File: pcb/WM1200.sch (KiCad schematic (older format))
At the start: 0 parts

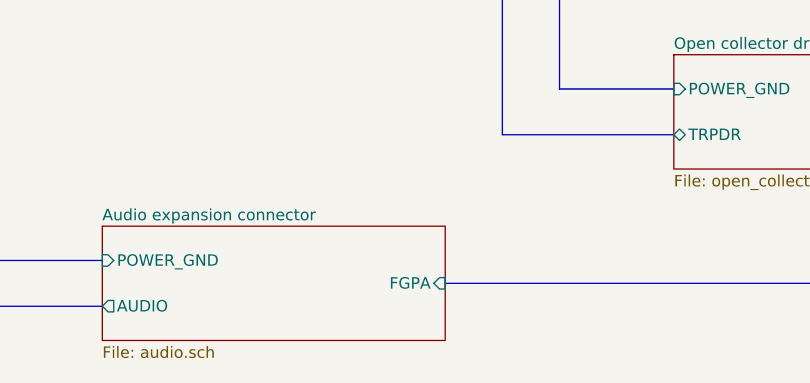
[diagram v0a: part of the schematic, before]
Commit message: bus name typo fixed on audio sheet
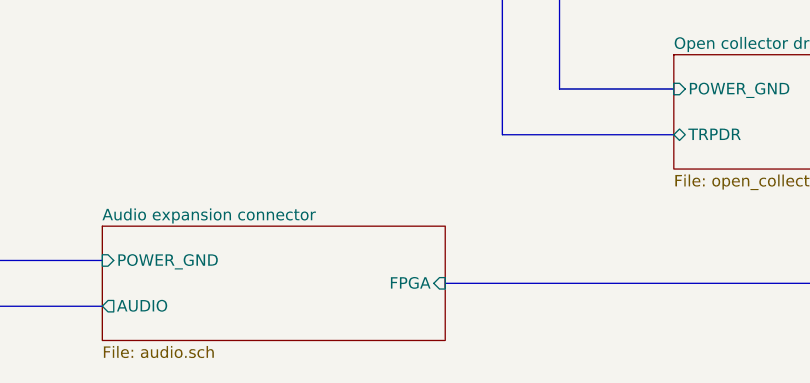
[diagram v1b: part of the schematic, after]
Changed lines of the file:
@@
 	5500 1150 5500 1650
-$Sheet
-S 3500 5250 1500 500
-U 5E5BC361
-F0 "Audio expansion connector" 50
-F1 "audio.sch" 50
-F2 "AUDIO" O L 3500 5600 50
-F3 "FGPA" I R 5000 5500 50
-F4 "POWER_GND" I L 3500 5400 50
-$EndSheet
 $Sheet
 S 6000 1500 1450 500
@@
 	3000 5400 3500 5400
 Connection ~ 3000 3750
+$Sheet
+S 3500 5250 1500 500
+U 5E5BC361
+F0 "Audio expansion connector" 50
+F1 "audio.sch" 50
+F2 "AUDIO" O L 3500 5600 50
+F3 "POWER_GND" I L 3500 5400 50
+F4 "FPGA" I R 5000 5500 50
+$EndSheet
 $EndSCHEMATC

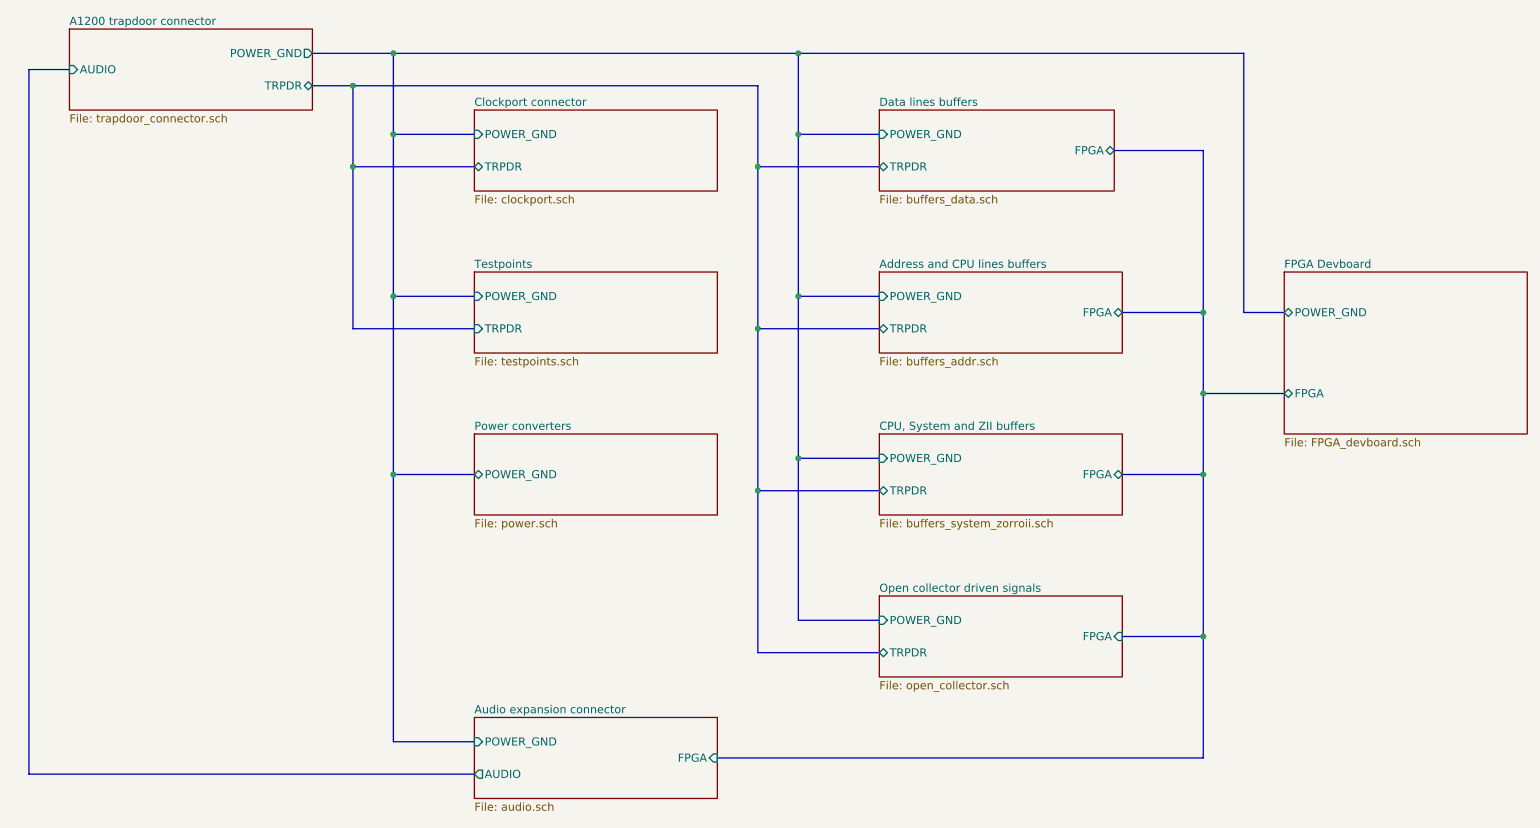
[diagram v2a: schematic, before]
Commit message: The scheme needs it's buses to be remade because of the way KiCad works, ok
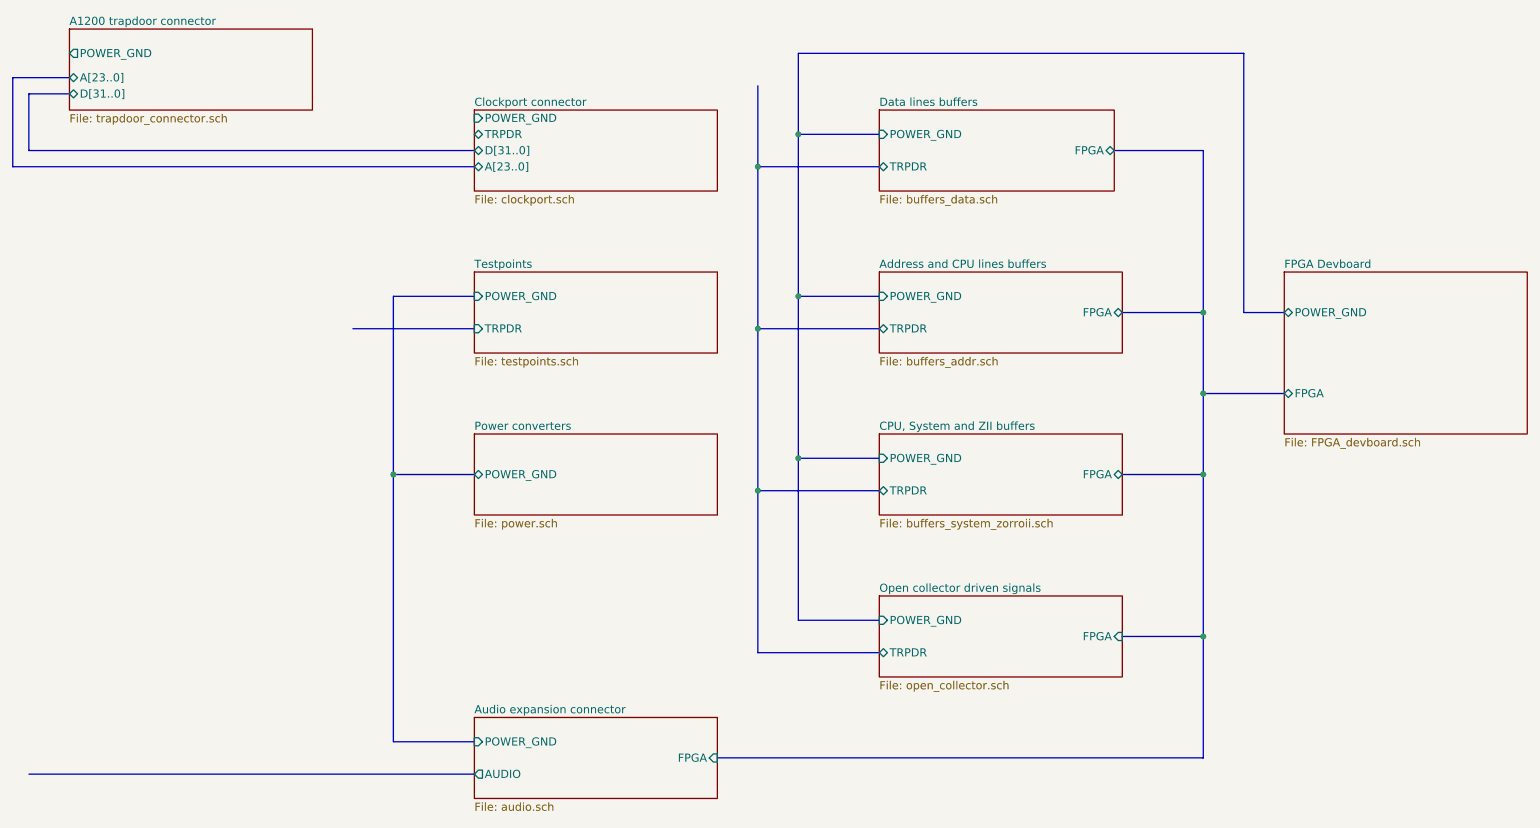
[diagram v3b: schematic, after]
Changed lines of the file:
@@
 F0 "A1200 trapdoor connector" 50
 F1 "trapdoor_connector.sch" 50
-F2 "AUDIO" I L 1000 1250 50
-F3 "POWER_GND" O R 2500 1150 50
-F4 "TRPDR" B R 2500 1350 50
-$EndSheet
-$Sheet
-S 3500 1500 1500 500
-U 5E55E8C3
-F0 "Clockport connector" 50
-F1 "clockport.sch" 50
-F2 "POWER_GND" I L 3500 1650 50
-F3 "TRPDR" B L 3500 1850 50
+F2 "POWER_GND" O L 1000 1150 50
+F3 "A[23..0]" B L 1000 1300 50
+F4 "D[31..0]" B L 1000 1400 50
 $EndSheet
 $Sheet
@@
 F3 "TRPDR" I L 3500 2850 50
 $EndSheet
-Wire Bus Line
-	3000 1650 3500 1650
 $Sheet
 S 6000 4500 1500 500
@@
 F4 "POWER_GND" I L 6000 3650 50
 $EndSheet
-Wire Bus Line
-	1000 1250 750  1250
-Wire Bus Line
-	750  1250 750  5600
 Wire Bus Line
 	750  5600 3500 5600
@@
 	8000 3250 8000 3750
 Wire Bus Line
-	3000 1650 3000 2650
-Wire Bus Line
 	5500 4650 6000 4650
 Wire Bus Line
@@
 	3500 2650 3000 2650
 Wire Bus Line
-	2500 1150 3000 1150
-Wire Bus Line
 	5500 1150 8250 1150
 Wire Bus Line
 	8250 1150 8250 2750
-Connection ~ 5500 1150
-Wire Bus Line
-	2750 1350 5250 1350
-Wire Bus Line
-	3000 1650 3000 1150
-Connection ~ 3000 1650
-Connection ~ 3000 1150
-Wire Bus Line
-	3000 1150 5500 1150
 Wire Bus Line
 	3000 2650 3000 3750
 Wire Bus Line
 	3000 3750 3500 3750
-Connection ~ 3000 2650
 Wire Bus Line
 	3000 3750 3000 5400
@@
 F4 "FPGA" I R 5000 5500 50
 $EndSheet
+$Sheet
+S 3500 1500 1500 500
+U 5E55E8C3
+F0 "Clockport connector" 50
+F1 "clockport.sch" 50
+F2 "POWER_GND" I L 3500 1550 50
+F3 "TRPDR" B L 3500 1650 50
+F4 "D[31..0]" B L 3500 1750 50
+F5 "A[23..0]" B L 3500 1850 50
+$EndSheet
 Wire Bus Line
-	2750 1850 3500 1850
+	1000 1300 650  1300
 Wire Bus Line
-	2750 1850 2750 2850
-Connection ~ 2750 1850
+	650  1300 650  1850
 Wire Bus Line
-	2750 1850 2750 1350
-Connection ~ 2750 1350
+	650  1850 3500 1850
 Wire Bus Line
-	2500 1350 2750 1350
+	1000 1400 750  1400
+Wire Bus Line
+	750  1400 750  1750
+Wire Bus Line
+	750  1750 3500 1750
 $EndSCHEMATC

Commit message: wip commit (sync work between pc's)
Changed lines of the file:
@@
 $EndDescr
-$Sheet
-S 1000 1000 1500 500
-U 5E6286C8
-F0 "A1200 trapdoor connector" 50
-F1 "trapdoor_connector.sch" 50
-F2 "POWER_GND" O L 1000 1150 50
-F3 "A[23..0]" B L 1000 1300 50
-F4 "D[31..0]" B L 1000 1400 50
-$EndSheet
 $Sheet
 S 3500 2500 1500 500
@@
 F5 "A[23..0]" B L 3500 1850 50
 $EndSheet
-Wire Bus Line
-	1000 1300 650  1300
-Wire Bus Line
-	650  1300 650  1850
-Wire Bus Line
-	650  1850 3500 1850
-Wire Bus Line
-	1000 1400 750  1400
-Wire Bus Line
-	750  1400 750  1750
-Wire Bus Line
-	750  1750 3500 1750
+$Sheet
+S 1000 1000 1500 2500
+U 5E6286C8
+F0 "A1200 trapdoor connector" 50
+F1 "trapdoor_connector.sch" 50
+F2 "A[23..0]" B R 2500 1100 50
+F3 "D[31..0]" B R 2500 1200 50
+F4 "_IPL[2..0]" B R 2500 1400 50
+F5 "SIZE[1..0]" B R 2500 1500 50
+F6 "_DSACK[1..0]" B R 2500 1600 50
+F7 "FC[2..0]" B R 2500 1700 50
+F8 "_RST" B R 2500 1800 50
+F9 "_HLT" B R 2500 1900 50
+F10 "_AS" B R 2500 2000 50
+F11 "_DS" B R 2500 2100 50
+F12 "R_W" B R 2500 2200 50
+F13 "_BERR" B R 2500 2300 50
+F14 "CPUCLK_A" B R 2500 2400 50
+F15 "E_CLOCK" B R 2500 2500 50
+F16 "_BR" B R 2500 2600 50
+F17 "_BOSS" B R 2500 2700 50
+F18 "CCKA" B R 2500 2800 50
+F19 "_RESET" B R 2500 2900 50
+F20 "_SPARECS" B R 2500 3000 50
+F21 "_RTCCS" B R 2500 3100 50
+F22 "_KBRESET" B R 2500 3200 50
+F23 "_IORD" B R 2500 3300 50
+F24 "AUDIO_RIGHT" B R 2500 3400 50
+F25 "AUDIO_LEFT" B L 1000 3200 50
+F26 "AUDIO_GND" B L 1000 3100 50
+F27 "_INT6" B L 1000 3000 50
+F28 "_INT2" B L 1000 2900 50
+F29 "_OVR" B L 1000 2800 50
+F30 "_IOWR" B L 1000 2700 50
+$EndSheet
 $EndSCHEMATC

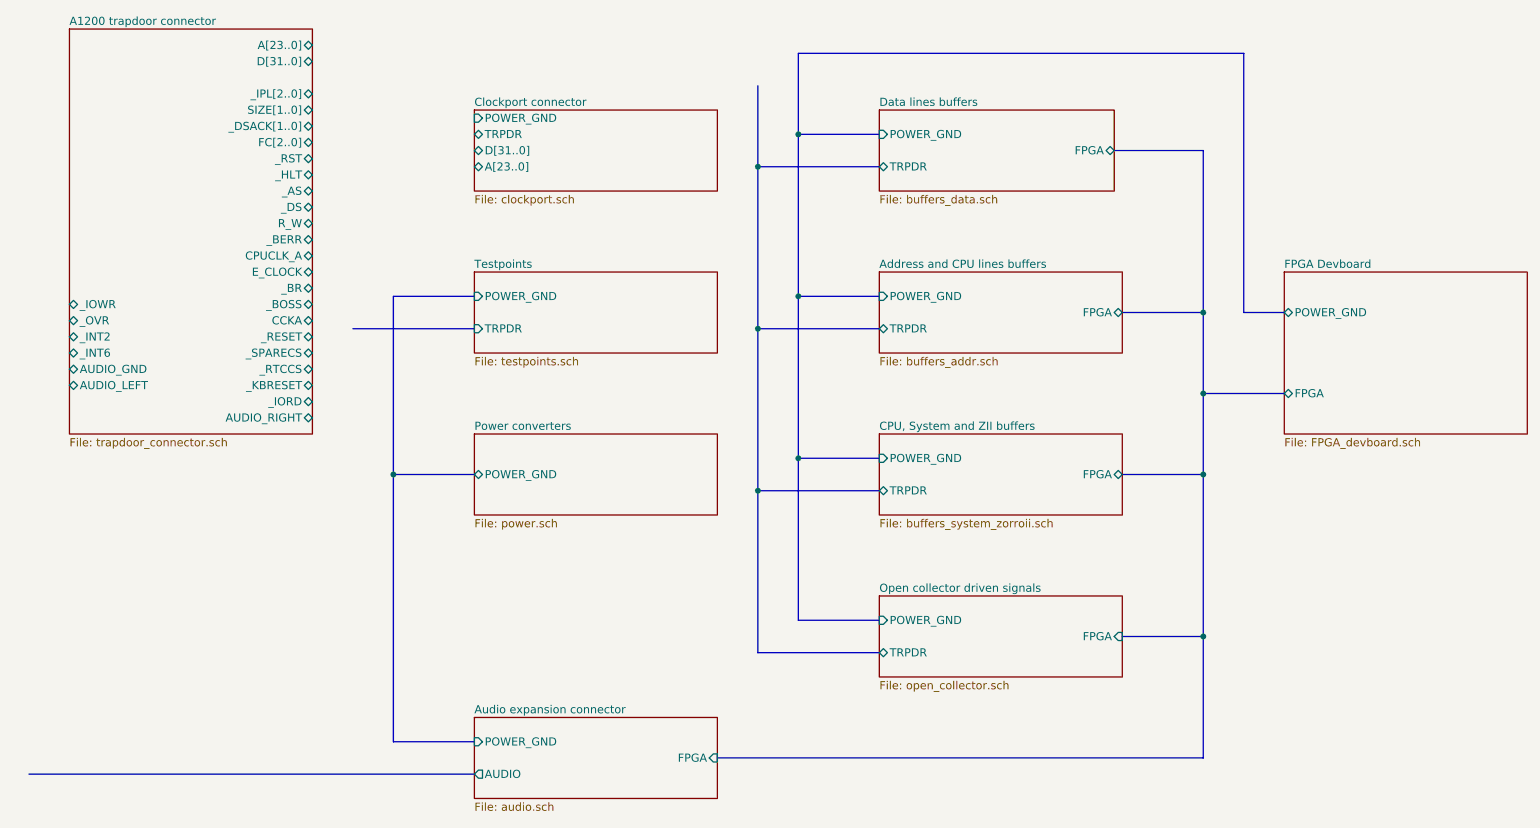
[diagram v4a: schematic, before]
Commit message: ok, we are using global labels now
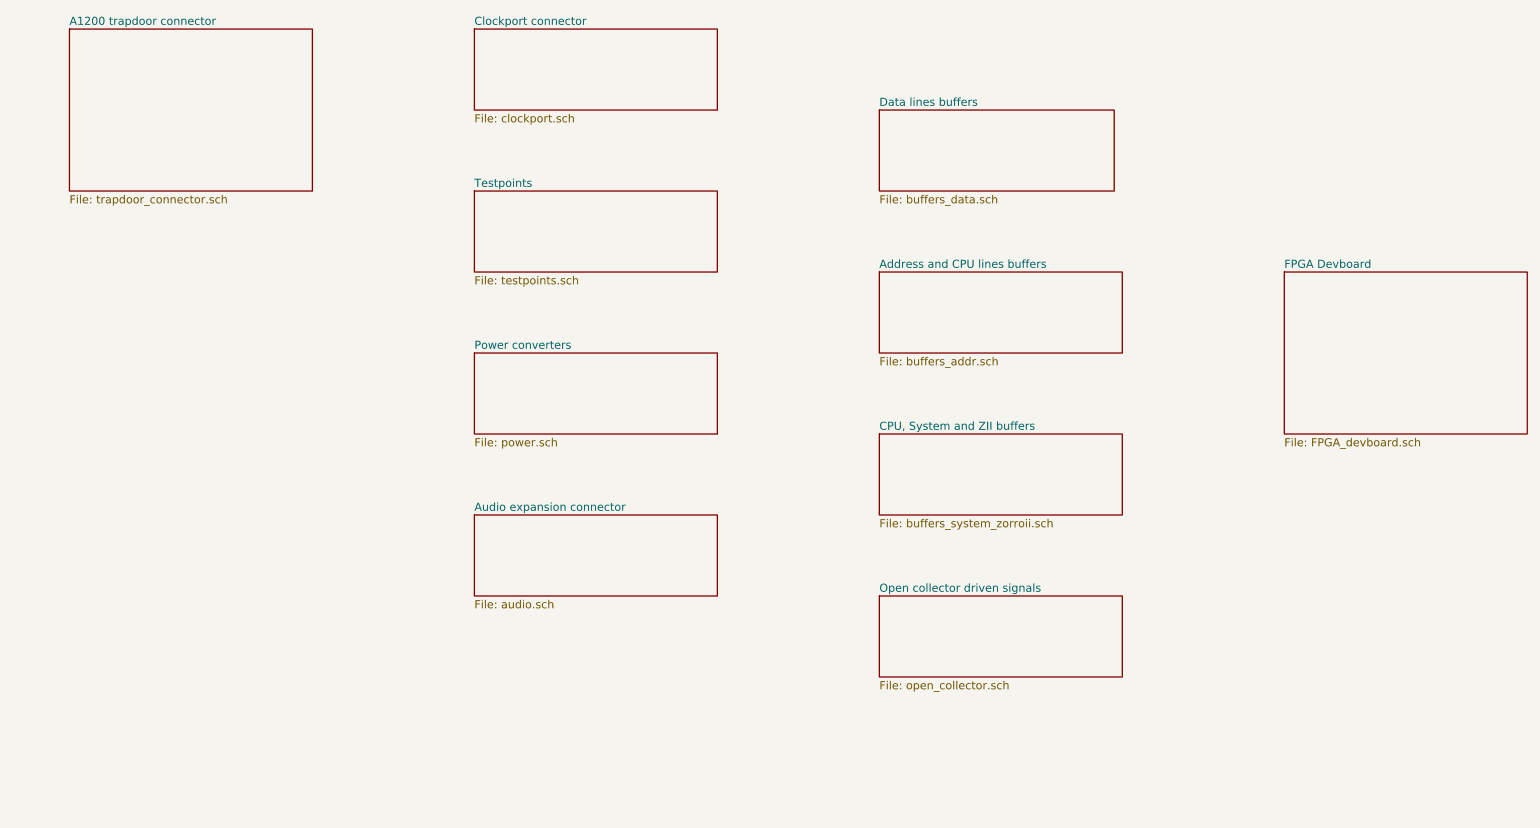
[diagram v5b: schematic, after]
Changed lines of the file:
@@
 $EndDescr
 $Sheet
-S 3500 2500 1500 500
+S 3500 2000 1500 500
 U 5E5B86AA
 F0 "Testpoints" 50
 F1 "testpoints.sch" 50
-F2 "POWER_GND" I L 3500 2650 50
-F3 "TRPDR" I L 3500 2850 50
+$EndSheet
+$Sheet
+S 6000 1500 1450 500
+U 5E5B89F7
+F0 "Data lines buffers" 50
+F1 "buffers_data.sch" 50
+$EndSheet
+$Sheet
+S 6000 2500 1500 500
+U 5E78104B
+F0 "Address and CPU lines buffers" 50
+F1 "buffers_addr.sch" 50
+$EndSheet
+$Sheet
+S 6000 3500 1500 500
+U 5E78B6EB
+F0 "CPU, System and ZII buffers" 50
+F1 "buffers_system_zorroii.sch" 50
+$EndSheet
+$Sheet
+S 3500 3000 1500 500
+U 5E87139E
+F0 "Power converters" 50
+F1 "power.sch" 50
+$EndSheet
+$Sheet
+S 3500 4000 1500 500
+U 5E5BC361
+F0 "Audio expansion connector" 50
+F1 "audio.sch" 50
+$EndSheet
+$Sheet
+S 1000 1000 1500 1000
+U 5E6286C8
+F0 "A1200 trapdoor connector" 50
+F1 "trapdoor_connector.sch" 50
+$EndSheet
+$Sheet
+S 3500 1000 1500 500
+U 5E55E8C3
+F0 "Clockport connector" 50
+F1 "clockport.sch" 50
 $EndSheet
 $Sheet
@@
 F0 "Open collector driven signals" 50
 F1 "open_collector.sch" 50
-F2 "POWER_GND" I L 6000 4650 50
-F3 "TRPDR" B L 6000 4850 50
-F4 "FPGA" I R 7500 4750 50
 $EndSheet
 $Sheet
@@
 F0 "FPGA Devboard" 50
 F1 "FPGA_devboard.sch" 50
-F2 "FPGA" B L 8500 3250 50
-F3 "POWER_GND" B L 8500 2750 50
-$EndSheet
-Wire Bus Line
-	5500 1150 5500 1650
-$Sheet
-S 6000 1500 1450 500
-U 5E5B89F7
-F0 "Data lines buffers" 50
-F1 "buffers_data.sch" 50
-F2 "FPGA" B R 7450 1750 50
-F3 "TRPDR" B L 6000 1850 50
-F4 "POWER_GND" I L 6000 1650 50
-$EndSheet
-$Sheet
-S 6000 2500 1500 500
-U 5E78104B
-F0 "Address and CPU lines buffers" 50
-F1 "buffers_addr.sch" 50
-F2 "FPGA" B R 7500 2750 50
-F3 "TRPDR" B L 6000 2850 50
-F4 "POWER_GND" I L 6000 2650 50
-$EndSheet
-$Sheet
-S 6000 3500 1500 500
-U 5E78B6EB
-F0 "CPU, System and ZII buffers" 50
-F1 "buffers_system_zorroii.sch" 50
-F2 "FPGA" B R 7500 3750 50
-F3 "TRPDR" B L 6000 3850 50
-F4 "POWER_GND" I L 6000 3650 50
-$EndSheet
-Wire Bus Line
-	750  5600 3500 5600
-Wire Bus Line
-	5250 1350 5250 1850
-Wire Bus Line
-	5500 1650 6000 1650
-Connection ~ 5500 1650
-Wire Bus Line
-	5500 1650 5500 2650
-Wire Bus Line
-	6000 1850 5250 1850
-Connection ~ 5250 1850
-Wire Bus Line
-	5250 1850 5250 2850
-Wire Bus Line
-	6000 2650 5500 2650
-Connection ~ 5500 2650
-Wire Bus Line
-	6000 2850 5250 2850
-Connection ~ 5250 2850
-Wire Bus Line
-	5250 2850 5250 3850
-Wire Bus Line
-	6000 3650 5500 3650
-Wire Bus Line
-	5500 2650 5500 3650
-Connection ~ 5500 3650
-Wire Bus Line
-	6000 3850 5250 3850
-Connection ~ 5250 3850
-Wire Bus Line
-	5250 3850 5250 4850
-Wire Bus Line
-	7450 1750 8000 1750
-Wire Bus Line
-	7500 2750 8000 2750
-Wire Bus Line
-	8000 1750 8000 2750
-Connection ~ 8000 2750
-Wire Bus Line
-	8000 2750 8000 3250
-Wire Bus Line
-	7500 3750 8000 3750
-Connection ~ 8000 3750
-Wire Bus Line
-	5000 5500 8000 5500
-Wire Bus Line
-	8000 3750 8000 4750
-$Sheet
-S 3500 3500 1500 500
-U 5E87139E
-F0 "Power converters" 50
-F1 "power.sch" 50
-F2 "POWER_GND" B L 3500 3750 50
-$EndSheet
-Wire Bus Line
-	8250 2750 8500 2750
-Wire Bus Line
-	8500 3250 8000 3250
-Connection ~ 8000 3250
-Wire Bus Line
-	8000 3250 8000 3750
-Wire Bus Line
-	5500 4650 6000 4650
-Wire Bus Line
-	5500 3650 5500 4650
-Wire Bus Line
-	6000 4850 5250 4850
-Wire Bus Line
-	7500 4750 8000 4750
-Connection ~ 8000 4750
-Wire Bus Line
-	8000 4750 8000 5500
-Wire Bus Line
-	2750 2850 3500 2850
-Wire Bus Line
-	3500 2650 3000 2650
-Wire Bus Line
-	5500 1150 8250 1150
-Wire Bus Line
-	8250 1150 8250 2750
-Wire Bus Line
-	3000 2650 3000 3750
-Wire Bus Line
-	3000 3750 3500 3750
-Wire Bus Line
-	3000 3750 3000 5400
-Wire Bus Line
-	3000 5400 3500 5400
-Connection ~ 3000 3750
-$Sheet
-S 3500 5250 1500 500
-U 5E5BC361
-F0 "Audio expansion connector" 50
-F1 "audio.sch" 50
-F2 "AUDIO" O L 3500 5600 50
-F3 "POWER_GND" I L 3500 5400 50
-F4 "FPGA" I R 5000 5500 50
-$EndSheet
-$Sheet
-S 3500 1500 1500 500
-U 5E55E8C3
-F0 "Clockport connector" 50
-F1 "clockport.sch" 50
-F2 "POWER_GND" I L 3500 1550 50
-F3 "TRPDR" B L 3500 1650 50
-F4 "D[31..0]" B L 3500 1750 50
-F5 "A[23..0]" B L 3500 1850 50
-$EndSheet
-$Sheet
-S 1000 1000 1500 2500
-U 5E6286C8
-F0 "A1200 trapdoor connector" 50
-F1 "trapdoor_connector.sch" 50
-F2 "A[23..0]" B R 2500 1100 50
-F3 "D[31..0]" B R 2500 1200 50
-F4 "_IPL[2..0]" B R 2500 1400 50
-F5 "SIZE[1..0]" B R 2500 1500 50
-F6 "_DSACK[1..0]" B R 2500 1600 50
-F7 "FC[2..0]" B R 2500 1700 50
-F8 "_RST" B R 2500 1800 50
-F9 "_HLT" B R 2500 1900 50
-F10 "_AS" B R 2500 2000 50
-F11 "_DS" B R 2500 2100 50
-F12 "R_W" B R 2500 2200 50
-F13 "_BERR" B R 2500 2300 50
-F14 "CPUCLK_A" B R 2500 2400 50
-F15 "E_CLOCK" B R 2500 2500 50
-F16 "_BR" B R 2500 2600 50
-F17 "_BOSS" B R 2500 2700 50
-F18 "CCKA" B R 2500 2800 50
-F19 "_RESET" B R 2500 2900 50
-F20 "_SPARECS" B R 2500 3000 50
-F21 "_RTCCS" B R 2500 3100 50
-F22 "_KBRESET" B R 2500 3200 50
-F23 "_IORD" B R 2500 3300 50
-F24 "AUDIO_RIGHT" B R 2500 3400 50
-F25 "AUDIO_LEFT" B L 1000 3200 50
-F26 "AUDIO_GND" B L 1000 3100 50
-F27 "_INT6" B L 1000 3000 50
-F28 "_INT2" B L 1000 2900 50
-F29 "_OVR" B L 1000 2800 50
-F30 "_IOWR" B L 1000 2700 50
 $EndSheet
 $EndSCHEMATC

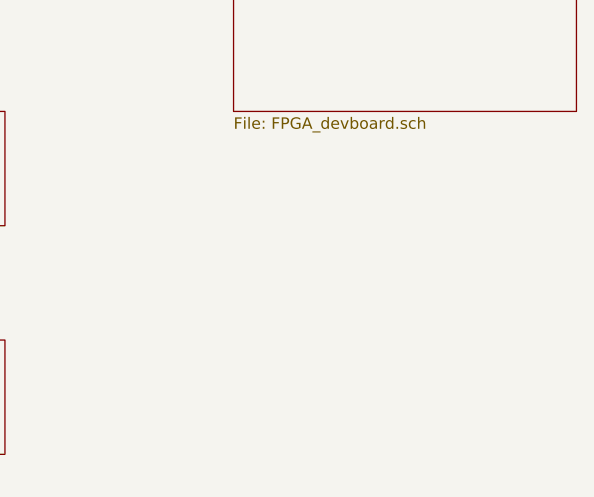
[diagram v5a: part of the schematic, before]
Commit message: hdmi list added
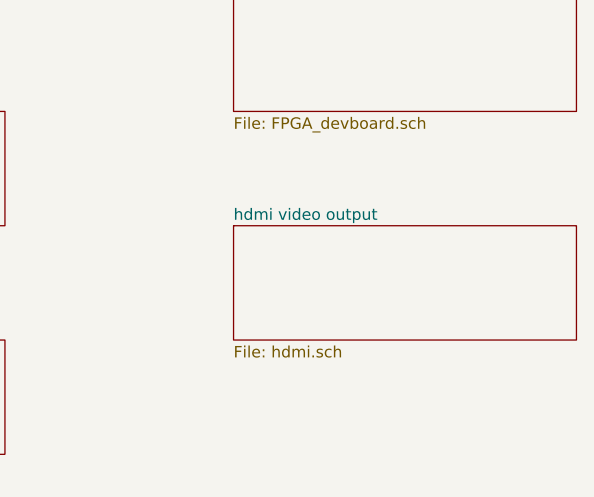
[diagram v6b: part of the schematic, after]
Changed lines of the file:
@@
 $Descr A4 11693 8268
 encoding utf-8
-Sheet 1 11
+Sheet 1 12
 Title "WishMaster 1200"
 Date ""
@@
 F1 "FPGA_devboard.sch" 50
 $EndSheet
+$Sheet
+S 8500 4000 1500 500
+U 5E5A0969
+F0 "hdmi video output" 50
+F1 "hdmi.sch" 50
+$EndSheet
 $EndSCHEMATC
